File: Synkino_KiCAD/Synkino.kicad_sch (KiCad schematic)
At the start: 171 parts, among them J1 Pwr, J10 EYE8_OUT, J11 EYE4_OUT, J12 Eye, J13 EYE5_OUT, J2 Eye, J3 3.5mm, J4 Micro_SD_Card_Det_Hirose_DM3AT, J5 EYE1_OUT, J6 EYE6_OUT, J7 EYE2_OUT, J8 EYE7_OUT, J9 EYE3_OUT, Q1 IRF7319, Q2 BC847 o. SS8050, Q3 IRLML2244, SW1 Power, SW2 Encoder, SW3 Reset, U1 ME6210A50PG, U10 ATMEGA328P-AU, U11 QRE1113GR, U12 QRE1113GR, U13 QRE1113GR, U14 QRE1113GR, U15 QRE1113GR, U16 QRE1113GR, U17 24LC256, U18 QRE1113GR, U2 ATMEGA328P-AU, U3 74HC4050, U4 SPIOLED128x64, U5 AP7312-1833W6-7, U6 74HC14, U7 VS1053B, U8 GS3005, U9 QRE1113GR, X1 FTDIconn, X2 ICSP, X3 FTDIconn, X4 ICSP, Y1 16Mhz, Y2 12.288MHz, Y3 16Mhz

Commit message: Moving Eyes to separate Board to allow V-Cuts instead of Mousebites
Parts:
- R31, R32, R33, R34, R38, R39, R40, R41, R42, R43, R44, R45, R46, R48, R50, R52, U11, U12, U13, U14, U15, U16, U18, U9: now left out of the parts list
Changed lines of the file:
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@@
 		(unit 1)
 		(exclude_from_sim no)
-		(in_bom yes)
-		(on_board yes)
+		(in_bom no)
+		(on_board no)
 		(dnp no)
 		(property "Reference" "U11"
@@
 		(unit 1)
 		(exclude_from_sim no)
-		(in_bom yes)
-		(on_board yes)
+		(in_bom no)
+		(on_board no)
 		(dnp no)
 		(property "Reference" "R33"
@@
 		(unit 1)
 		(exclude_from_sim no)
-		(in_bom yes)
-		(on_board yes)
+		(in_bom no)
+		(on_board no)
 		(dnp no)
 		(property "Reference" "R34"
@@
 		(exclude_from_sim no)
 		(in_bom no)
-		(on_board yes)
+		(on_board no)
 		(dnp no)
 		(property "Reference" "J7"
@@
 		(unit 1)
 		(exclude_from_sim no)
-		(in_bom yes)
-		(on_board yes)
+		(in_bom no)
+		(on_board no)
 		(dnp no)
 		(property "Reference" "U9"
@@
 		(unit 1)
 		(exclude_from_sim no)
-		(in_bom yes)
-		(on_board yes)
+		(in_bom no)
+		(on_board no)
 		(dnp no)
 		(property "Reference" "R31"
@@
 		(unit 1)
 		(exclude_from_sim no)
-		(in_bom yes)
-		(on_board yes)
+		(in_bom no)
+		(on_board no)
 		(dnp no)
 		(property "Reference" "R38"
@@
 		(exclude_from_sim no)
 		(in_bom no)
-		(on_board yes)
+		(on_board no)
 		(dnp no)
 		(property "Reference" "J5"
@@
 		(unit 1)
 		(exclude_from_sim no)
-		(in_bom yes)
-		(on_board yes)
+		(in_bom no)
+		(on_board no)
 		(dnp no)
 		(property "Reference" "U16"
@@
 		(unit 1)
 		(exclude_from_sim no)
-		(in_bom yes)
-		(on_board yes)
+		(in_bom no)
+		(on_board no)
 		(dnp no)
 		(property "Reference" "R46"
@@
 		(unit 1)
 		(exclude_from_sim no)
-		(in_bom yes)
-		(on_board yes)
+		(in_bom no)
+		(on_board no)
 		(dnp no)
 		(property "Reference" "R48"
@@
 		(exclude_from_sim no)
 		(in_bom no)
-		(on_board yes)
+		(on_board no)
 		(dnp no)
 		(property "Reference" "J11"
@@
 		(unit 1)
 		(exclude_from_sim no)
-		(in_bom yes)
-		(on_board yes)
+		(in_bom no)
+		(on_board no)
 		(dnp no)
 		(property "Reference" "U14"
@@
 		(unit 1)
 		(exclude_from_sim no)
-		(in_bom yes)
-		(on_board yes)
+		(in_bom no)
+		(on_board no)
 		(dnp no)
 		(property "Reference" "R42"
@@
 		(unit 1)
 		(exclude_from_sim no)
-		(in_bom yes)
-		(on_board yes)
+		(in_bom no)
+		(on_board no)
 		(dnp no)
 		(property "Reference" "R44"
@@
 		(exclude_from_sim no)
 		(in_bom no)
-		(on_board yes)
+		(on_board no)
 		(dnp no)
 		(property "Reference" "J9"
@@
 		(unit 1)
 		(exclude_from_sim no)
-		(in_bom yes)
-		(on_board yes)
+		(in_bom no)
+		(on_board no)
 		(dnp no)
 		(property "Reference" "U18"
@@
 		(unit 1)
 		(exclude_from_sim no)
-		(in_bom yes)
-		(on_board yes)
+		(in_bom no)
+		(on_board no)
 		(dnp no)
 		(property "Reference" "R50"
@@
 		(unit 1)
 		(exclude_from_sim no)
-		(in_bom yes)
-		(on_board yes)
+		(in_bom no)
+		(on_board no)
 		(dnp no)
 		(property "Reference" "R52"
@@
 		(exclude_from_sim no)
 		(in_bom no)
-		(on_board yes)
+		(on_board no)
 		(dnp no)
 		(property "Reference" "J13"
@@
 		(unit 1)
 		(exclude_from_sim no)
-		(in_bom yes)
-		(on_board yes)
+		(in_bom no)
+		(on_board no)
 		(dnp no)
 		(property "Reference" "U13"
@@
 		(unit 1)
 		(exclude_from_sim no)
-		(in_bom yes)
-		(on_board yes)
+		(in_bom no)
+		(on_board no)
 		(dnp no)
 		(property "Reference" "R40"
@@
 		(unit 1)
 		(exclude_from_sim no)
-		(in_bom yes)
-		(on_board yes)
+		(in_bom no)
+		(on_board no)
 		(dnp no)
 		(property "Reference" "R41"
@@
 		(exclude_from_sim no)
 		(in_bom no)
-		(on_board yes)
+		(on_board no)
 		(dnp no)
 		(property "Reference" "J8"
@@
 		(unit 1)
 		(exclude_from_sim no)
-		(in_bom yes)
-		(on_board yes)
+		(in_bom no)
+		(on_board no)
 		(dnp no)
 		(property "Reference" "U12"
@@
 		(unit 1)
 		(exclude_from_sim no)
-		(in_bom yes)
-		(on_board yes)
+		(in_bom no)
+		(on_board no)
 		(dnp no)
 		(property "Reference" "R32"
@@
 		(unit 1)
 		(exclude_from_sim no)
-		(in_bom yes)
-		(on_board yes)
+		(in_bom no)
+		(on_board no)
 		(dnp no)
 		(property "Reference" "R39"
@@
 		(exclude_from_sim no)
 		(in_bom no)
-		(on_board yes)
+		(on_board no)
 		(dnp no)
 		(property "Reference" "J6"
@@
 		(unit 1)
 		(exclude_from_sim no)
-		(in_bom yes)
-		(on_board yes)
+		(in_bom no)
+		(on_board no)
 		(dnp no)
 		(property "Reference" "U15"
@@
 		(unit 1)
 		(exclude_from_sim no)
-		(in_bom yes)
-		(on_board yes)
+		(in_bom no)
+		(on_board no)
 		(dnp no)
 		(property "Reference" "R43"
@@
 		(unit 1)
 		(exclude_from_sim no)
-		(in_bom yes)
-		(on_board yes)
+		(in_bom no)
+		(on_board no)
 		(dnp no)
 		(property "Reference" "R45"
@@
 		(exclude_from_sim no)
 		(in_bom no)
-		(on_board yes)
+		(on_board no)
 		(dnp no)
 		(property "Reference" "J10"

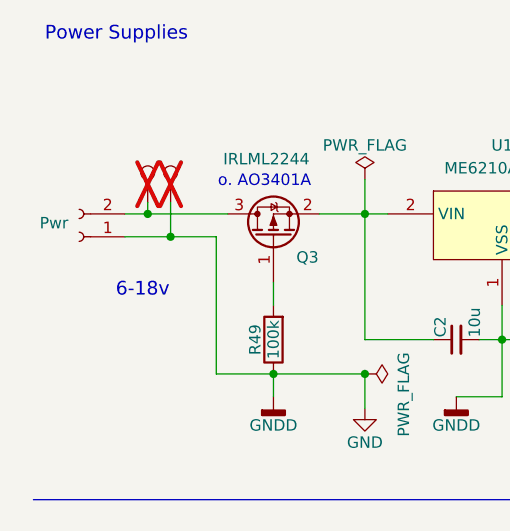
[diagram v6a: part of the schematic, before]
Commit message: Adding Battery Holder, Battery connector
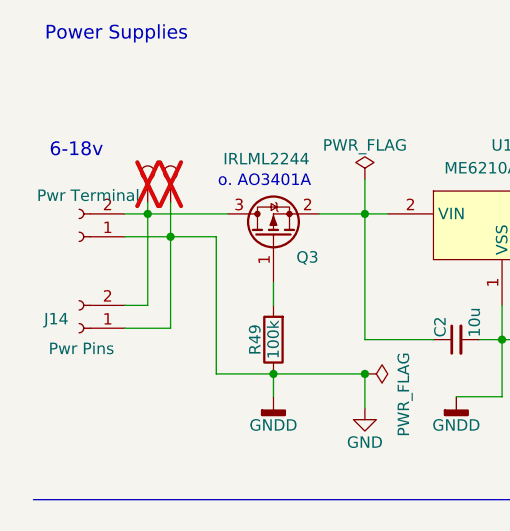
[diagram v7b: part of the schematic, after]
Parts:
- added J14: Pwr Pins, Connector_PinHeader_2.54mm:PinHeader_1x02_P2.54mm_Vertical, symbol Connector:Conn_01x02_Socket
- J1: value Pwr -> Pwr Terminal
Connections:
- net GND: now also J14.1 (Pin_1)
- net at J1.2 (Pin_2), Q3.3 (D), TP5.1: now also J14.2 (Pin_2)
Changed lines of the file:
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@@
 	(wire
 		(pts
+			(xy 22.86 44.45) (xy 25.4 44.45)
+		)
+		(stroke
+			(width 0)
+			(type default)
+		)
+	)
+	(wire
+		(pts
 			(xy 125.73 29.21) (xy 125.73 34.29)
 		)
@@
 	(wire
 		(pts
+			(xy 22.86 46.99) (xy 27.94 46.99)
+		)
+		(stroke
+			(width 0)
+			(type default)
+		)
+	)
+	(wire
+		(pts
 			(xy 303.53 43.18) (xy 307.34 43.18)
 		)
@@
 	(wire
 		(pts
+			(xy 27.94 46.99) (xy 27.94 36.83)
+		)
+		(stroke
+			(width 0)
+			(type default)
+		)
+	)
+	(wire
+		(pts
 			(xy 374.65 62.23) (xy 372.11 62.23)
 		)
@@
 	(wire
 		(pts
+			(xy 25.4 44.45) (xy 25.4 34.29)
+		)
+		(stroke
+			(width 0)
+			(type default)
+		)
+	)
+	(wire
+		(pts
 			(xy 334.01 220.98) (xy 327.66 220.98)
 		)
@@
 	(text "6-18v\n"
 		(exclude_from_sim no)
-		(at 21.844 43.688 0)
+		(at 14.478 28.194 0)
 		(effects
 			(font
@@
 			)
 		)
-		(property "Value" "Pwr"
-			(at 14.986 35.306 0)
+		(property "Value" "Pwr Terminal"
+			(at 18.796 32.258 0)
 			(effects
 				(font
@@
 					(unit 1)
 				)
+			)
+		)
+	)
+	(symbol
+		(lib_id "Connector:Conn_01x02_Socket")
+		(at 17.78 46.99 180)
+		(unit 1)
+		(exclude_from_sim no)
+		(in_bom yes)
+		(on_board yes)
+		(dnp no)
+		(property "Reference" "J14"
+			(at 15.24 45.974 0)
+			(effects
+				(font
+					(size 1.27 1.27)
+				)
+			)
+		)
+		(property "Value" "Pwr Pins"
+			(at 18.034 49.276 0)
+			(effects
+				(font
+					(size 1.27 1.27)
+				)
+			)
+		)
+		(property "Footprint" "Connector_PinHeader_2.54mm:PinHeader_1x02_P2.54mm_Vertical"
+			(at 17.78 46.99 0)
+			(effects
+				(font
+					(size 1.27 1.27)
+				)
+				(hide yes)
+			)
+		)
+		(property "Datasheet" "~"
+			(at 17.78 46.99 0)
+			(effects
+				(font
+					(size 1.27 1.27)
+				)
+				(hide yes)
+			)
+		)
+		(property "Description" "Generic connector, single row, 01x02, script generated"
+			(at 17.78 46.99 0)
+			(effects
+				(font
+					(size 1.27 1.27)
+				)
+				(hide yes)
+			)
+		)
+		(pin "2"
+		)
+		(pin "1"
+		)
+		(instances
+			(project "Synkino"
+				(path "/9d4924d9-a2ad-42f2-a951-8d7a9cc74761"
+					(reference "J14")
+					(unit 1)
+				)

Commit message: Rev.H as ordered
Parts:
- D2: value LED_ALT -> LED_wh
- D3: value LED_ALT -> LED_re
- J14: now left out of the parts list
- Y2: Alternative (none) -> C251589
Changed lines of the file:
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@@
 			)
 		)
-		(property "Value" "LED_ALT"
+		(property "Value" "LED_wh"
 			(at 255.27 242.57 0)
 			(effects
@@
 			)
 		)
+		(property "Alternative" "C251589"
+			(at 173.99 105.41 0)
+			(effects
+				(font
+					(size 1.27 1.27)
+				)
+				(hide yes)
+			)
+		)
 		(pin "1"
 		)
@@
 			)
 		)
-		(property "Value" "LED_ALT"
+		(property "Value" "LED_re"
 			(at 260.35 223.52 0)
 			(effects
@@
 		(unit 1)
 		(exclude_from_sim no)
-		(in_bom yes)
-		(on_board yes)
+		(in_bom no)
+		(on_board no)
 		(dnp no)
 		(property "Reference" "J14"
@@
 					(size 1.27 1.27)
 				)
+				(hide yes)
 			)
 		)
